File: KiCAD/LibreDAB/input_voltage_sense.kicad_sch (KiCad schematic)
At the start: 5 parts, among them U701 MCP6486UT-E/LT

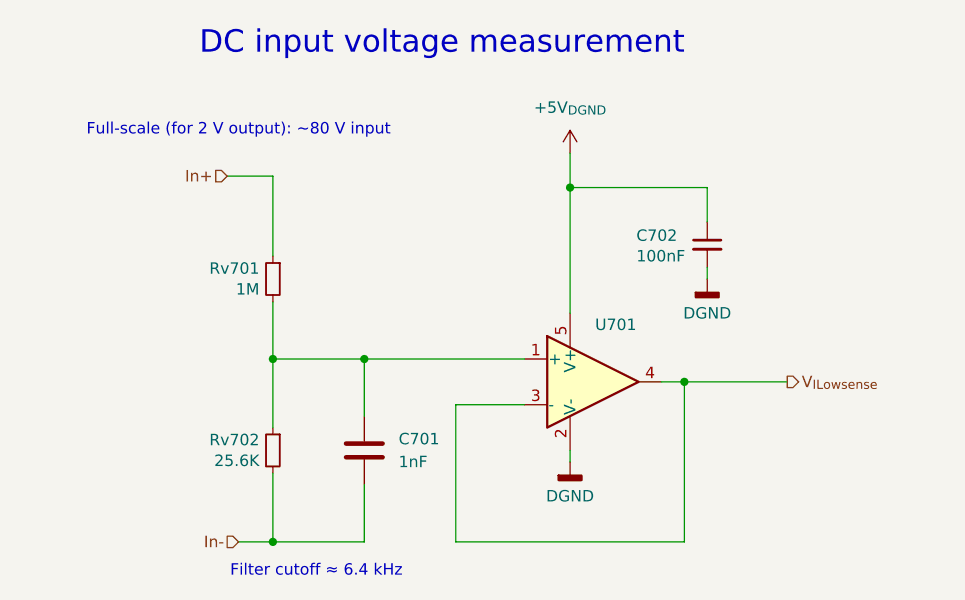
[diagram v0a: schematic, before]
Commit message: Initial kicad schematic draft
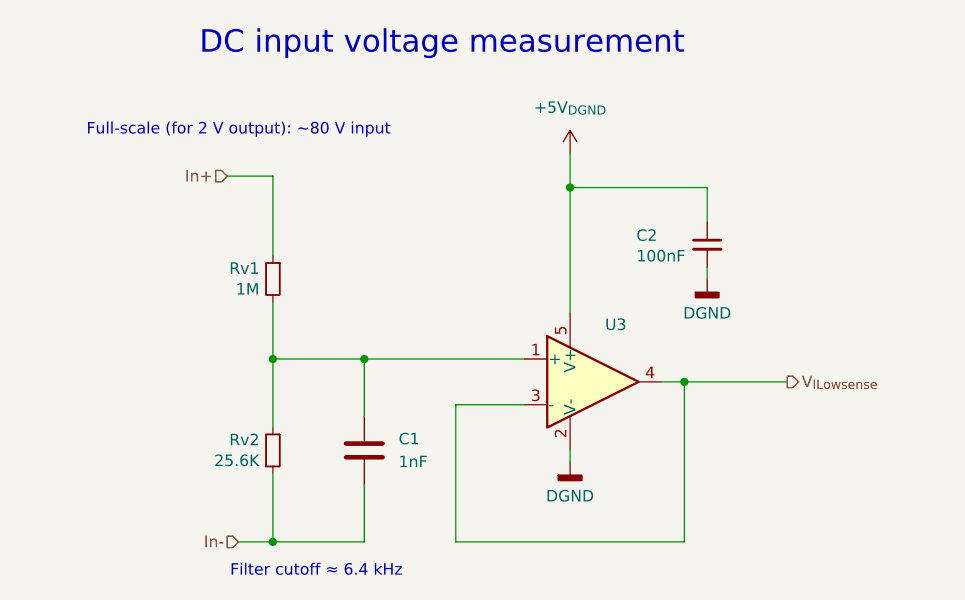
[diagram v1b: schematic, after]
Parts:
- renumbered C701 to C1, C702 to C2, Rv701 to Rv1, Rv702 to Rv2, U701 to U3
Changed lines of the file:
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@@
 		(on_board yes)
 		(dnp no)
-		(property "Reference" "#PWR0704"
+		(property "Reference" "#PWR03"
 			(at 113.03 88.9 0)
 			(effects
@@
 		)
 		(instances
-			(project "aluminum_pcb"
-				(path "/741fe409-f733-4088-8b5c-1042510db0b9/361c2cca-6888-4386-bbcc-54e5a005596e/dbec3990-da67-43cc-b337-37357147c21c"
-					(reference "#PWR0704")
+			(project "LibreDAB"
+				(path "/741fe409-f733-4088-8b5c-1042510db0b9/361c2cca-6888-4386-bbcc-54e5a005596e/2e3a4eb4-e720-44cb-b9f0-f85868bbc974"
+					(reference "#PWR03")
 					(unit 1)
 				)
@@
 		(on_board yes)
 		(dnp no)
-		(property "Reference" "#PWR0703"
+		(property "Reference" "#PWR02"
 			(at 97.79 109.22 0)
 			(effects
@@
 		)
 		(instances
-			(project "aluminum_pcb"
-				(path "/741fe409-f733-4088-8b5c-1042510db0b9/361c2cca-6888-4386-bbcc-54e5a005596e/dbec3990-da67-43cc-b337-37357147c21c"
-					(reference "#PWR0703")
+			(project "LibreDAB"
+				(path "/741fe409-f733-4088-8b5c-1042510db0b9/361c2cca-6888-4386-bbcc-54e5a005596e/2e3a4eb4-e720-44cb-b9f0-f85868bbc974"
+					(reference "#PWR02")
 					(unit 1)
 				)
@@
 		(dnp no)
 		(fields_autoplaced yes)
-		(property "Reference" "#PWR0702"
+		(property "Reference" "#PWR01"
 			(at 99.568 68.58 90)
 			(effects
@@
 		)
 		(instances
-			(project "aluminum_pcb"
-				(path "/741fe409-f733-4088-8b5c-1042510db0b9/361c2cca-6888-4386-bbcc-54e5a005596e/dbec3990-da67-43cc-b337-37357147c21c"
-					(reference "#PWR0702")
+			(project "LibreDAB"
+				(path "/741fe409-f733-4088-8b5c-1042510db0b9/361c2cca-6888-4386-bbcc-54e5a005596e/2e3a4eb4-e720-44cb-b9f0-f85868bbc974"
+					(reference "#PWR01")
 					(unit 1)
 				)
@@
 		(on_board yes)
 		(dnp no)
-		(property "Reference" "Rv702"
+		(property "Reference" "Rv2"
 			(at 63.2714 100.4316 0)
 			(effects
@@
 		)
 		(instances
-			(project "aluminum_pcb"
-				(path "/741fe409-f733-4088-8b5c-1042510db0b9/361c2cca-6888-4386-bbcc-54e5a005596e/dbec3990-da67-43cc-b337-37357147c21c"
-					(reference "Rv702")
+			(project "LibreDAB"
+				(path "/741fe409-f733-4088-8b5c-1042510db0b9/361c2cca-6888-4386-bbcc-54e5a005596e/2e3a4eb4-e720-44cb-b9f0-f85868bbc974"
+					(reference "Rv2")
 					(unit 1)
 				)
@@
 		(on_board yes)
 		(dnp no)
-		(property "Reference" "Rv701"
+		(property "Reference" "Rv1"
 			(at 63.2714 81.3816 0)
 			(effects
@@
 		)
 		(instances
-			(project "aluminum_pcb"
-				(path "/741fe409-f733-4088-8b5c-1042510db0b9/361c2cca-6888-4386-bbcc-54e5a005596e/dbec3990-da67-43cc-b337-37357147c21c"
-					(reference "Rv701")
+			(project "LibreDAB"
+				(path "/741fe409-f733-4088-8b5c-1042510db0b9/361c2cca-6888-4386-bbcc-54e5a005596e/2e3a4eb4-e720-44cb-b9f0-f85868bbc974"
+					(reference "Rv1")
 					(unit 1)
 				)
@@
 		(on_board yes)
 		(dnp no)
-		(property "Reference" "U701"
+		(property "Reference" "U3"
 			(at 102.87 87.63 0)
 			(effects
@@
 		)
 		(instances
-			(project "aluminum_pcb"
-				(path "/741fe409-f733-4088-8b5c-1042510db0b9/361c2cca-6888-4386-bbcc-54e5a005596e/dbec3990-da67-43cc-b337-37357147c21c"
-					(reference "U701")
+			(project "LibreDAB"
+				(path "/741fe409-f733-4088-8b5c-1042510db0b9/361c2cca-6888-4386-bbcc-54e5a005596e/2e3a4eb4-e720-44cb-b9f0-f85868bbc974"
+					(reference "U3")
 					(unit 1)
 				)
@@
 		(dnp no)
 		(fields_autoplaced yes)
-		(property "Reference" "C701"
+		(property "Reference" "C1"
 			(at 78.74 100.3299 0)
 			(effects
@@
 		)
 		(instances
-			(project ""
-				(path "/741fe409-f733-4088-8b5c-1042510db0b9/361c2cca-6888-4386-bbcc-54e5a005596e/dbec3990-da67-43cc-b337-37357147c21c"
-					(reference "C701")
+			(project "LibreDAB"
+				(path "/741fe409-f733-4088-8b5c-1042510db0b9/361c2cca-6888-4386-bbcc-54e5a005596e/2e3a4eb4-e720-44cb-b9f0-f85868bbc974"
+					(reference "C1")
 					(unit 1)
 				)
@@
 		(on_board yes)
 		(dnp no)
-		(property "Reference" "C702"
+		(property "Reference" "C2"
 			(at 105.156 77.724 0)
 			(effects
@@
 		)
 		(instances
-			(project "aluminum_pcb"
-				(path "/741fe409-f733-4088-8b5c-1042510db0b9/361c2cca-6888-4386-bbcc-54e5a005596e/dbec3990-da67-43cc-b337-37357147c21c"
-					(reference "C702")
-					(unit 1)
-				)
+			(project "LibreDAB"
+				(path "/741fe409-f733-4088-8b5c-1042510db0b9/361c2cca-6888-4386-bbcc-54e5a005596e/2e3a4eb4-e720-44cb-b9f0-f85868bbc974"
+					(reference "C2")
+					(unit 1)
+				)
